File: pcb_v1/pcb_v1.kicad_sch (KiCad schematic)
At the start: 13 parts, among them J3 Conn_01x07, SW1 SW_Push, SW2 SW_Push, U2 SRV05-4, U3 IQS624-3200-DNR

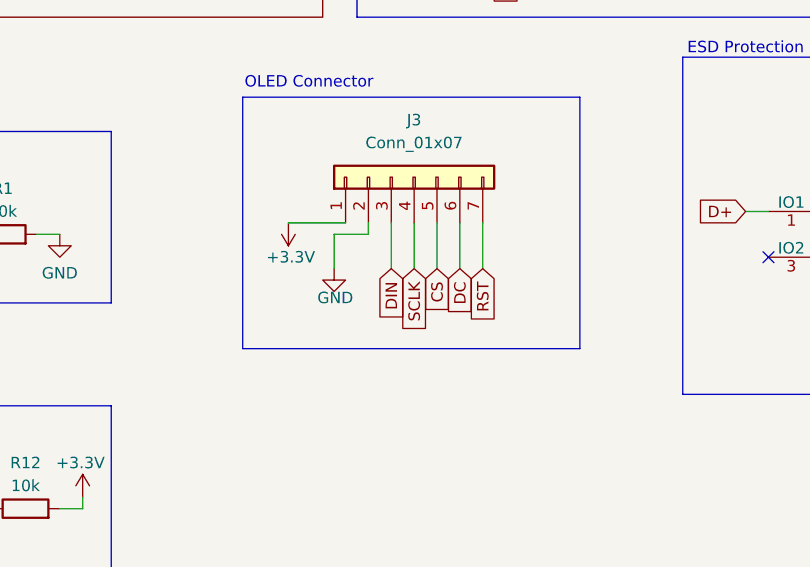
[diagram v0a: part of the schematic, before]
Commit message: Reverse polarity on pins
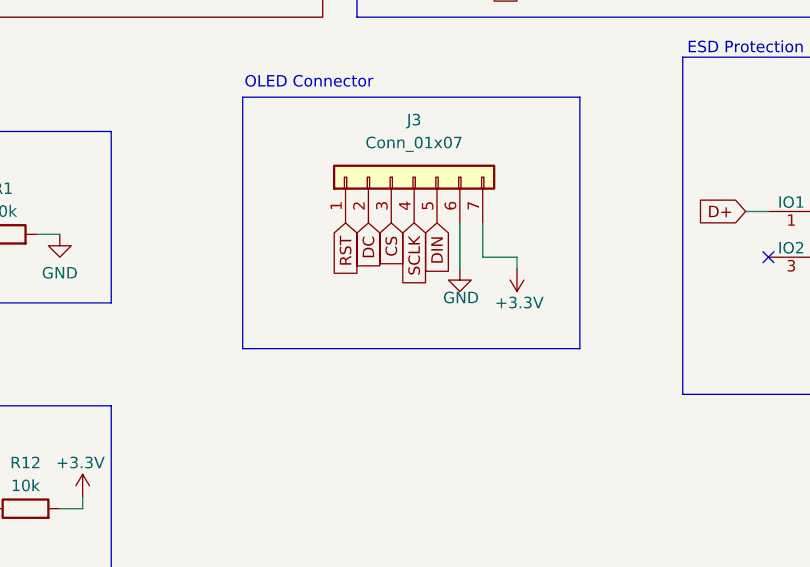
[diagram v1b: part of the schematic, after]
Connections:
- net +3.3V: now also J3.7 (Pin_7); no longer J3.1 (Pin_1)
- net CS: now also J3.3 (Pin_3); no longer J3.5 (Pin_5)
- net DC: now also J3.2 (Pin_2); no longer J3.6 (Pin_6)
- net DIN: now also J3.5 (Pin_5); no longer J3.3 (Pin_3)
- net GND: now also J3.6 (Pin_6); no longer J3.2 (Pin_2)
- net RST: now also J3.1 (Pin_1); no longer J3.7 (Pin_7)
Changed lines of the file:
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@@
 	(wire
 		(pts
-			(xy 196.85 149.86) (xy 196.85 144.78)
+			(xy 200.66 149.86) (xy 200.66 148.59)
 		)
 		(stroke
@@
 	(wire
 		(pts
+			(xy 200.66 148.59) (xy 196.85 148.59)
+		)
+		(stroke
+			(width 0)
+			(type default)
+		)
+	)
+	(wire
+		(pts
 			(xy 265.43 114.3) (xy 265.43 113.03)
 		)
@@
 	(wire
 		(pts
-			(xy 186.69 144.78) (xy 186.69 149.86)
-		)
-		(stroke
-			(width 0)
-			(type default)
-		)
-	)
-	(wire
-		(pts
 			(xy 186.69 101.6) (xy 199.39 101.6)
 		)
@@
 	(wire
 		(pts
-			(xy 191.77 149.86) (xy 191.77 144.78)
-		)
-		(stroke
-			(width 0)
-			(type default)
-		)
-	)
-	(wire
-		(pts
 			(xy 194.31 99.06) (xy 194.31 95.25)
 		)
@@
 	(wire
 		(pts
-			(xy 175.26 144.78) (xy 181.61 144.78)
-		)
-		(stroke
-			(width 0)
-			(type default)
-		)
-	)
-	(wire
-		(pts
 			(xy 241.3 158.75) (xy 247.65 158.75)
 		)
@@
 	(wire
 		(pts
-			(xy 180.34 146.05) (xy 184.15 146.05)
-		)
-		(stroke
-			(width 0)
-			(type default)
-		)
-	)
-	(wire
-		(pts
 			(xy 265.43 109.22) (xy 265.43 113.03)
 		)
@@
 	(wire
 		(pts
-			(xy 189.23 149.86) (xy 189.23 144.78)
-		)
-		(stroke
-			(width 0)
-			(type default)
-		)
-	)
-	(wire
-		(pts
 			(xy 205.74 96.52) (xy 204.47 96.52)
 		)
@@
 	(wire
 		(pts
-			(xy 184.15 146.05) (xy 184.15 144.78)
-		)
-		(stroke
-			(width 0)
-			(type default)
-		)
-	)
-	(wire
-		(pts
 			(xy 226.06 143.51) (xy 228.6 143.51)
 		)
@@
 	(wire
 		(pts
+			(xy 196.85 148.59) (xy 196.85 144.78)
+		)
+		(stroke
+			(width 0)
+			(type default)
+		)
+	)
+	(wire
+		(pts
 			(xy 139.7 173.99) (xy 139.7 176.53)
 		)
@@
 	(wire
 		(pts
-			(xy 180.34 149.86) (xy 180.34 146.05)
-		)
-		(stroke
-			(width 0)
-			(type default)
-		)
-	)
-	(wire
-		(pts
 			(xy 252.73 113.03) (xy 252.73 109.22)
 		)
@@
 			(width 0)
 			(type default)
-		)
-	)
-	(global_label "CS"
-		(shape input)
-		(at 191.77 149.86 270)
-		(fields_autoplaced yes)
-		(effects
-			(font
-				(size 1.27 1.27)
-			)
-			(justify right)
-		)
-		(property "Intersheetrefs" "${INTERSHEET_REFS}"
-			(at 191.77 155.3247 90)
-			(effects
-				(font
-					(size 1.27 1.27)
-				)
-				(justify right)
-				(hide yes)
-			)
 		)
 	)
@@
 		)
 	)
+	(global_label "DIN"
+		(shape input)
+		(at 191.77 144.78 270)
+		(fields_autoplaced yes)
+		(effects
+			(font
+				(size 1.27 1.27)
+			)
+			(justify right)
+		)
+		(property "Intersheetrefs" "${INTERSHEET_REFS}"
+			(at 191.77 150.9705 90)
+			(effects
+				(font
+					(size 1.27 1.27)
+				)
+				(justify right)
+				(hide yes)
+			)
+		)
+	)
 	(global_label "RDY"
 		(shape input)
@@
 		)
 	)
-	(global_label "DIN"
-		(shape input)
-		(at 186.69 149.86 270)
-		(fields_autoplaced yes)
-		(effects
-			(font
-				(size 1.27 1.27)
-			)
-			(justify right)
-		)
-		(property "Intersheetrefs" "${INTERSHEET_REFS}"
-			(at 186.69 156.0505 90)
-			(effects
-				(font
-					(size 1.27 1.27)
-				)
-				(justify right)
-				(hide yes)
-			)
-		)
-	)
 	(global_label "D+"
 		(shape input)
@@
 		)
 	)
-	(global_label "DC"
+	(global_label "CS"
 		(shape input)
-		(at 194.31 149.86 270)
+		(at 186.69 144.78 270)
 		(fields_autoplaced yes)
 		(effects
@@
 		)
 		(property "Intersheetrefs" "${INTERSHEET_REFS}"
-			(at 194.31 155.3852 90)
+			(at 186.69 150.2447 90)
+			(effects
+				(font
+					(size 1.27 1.27)
+				)
+				(justify right)
+				(hide yes)
+			)
+		)
+	)
+	(global_label "RST"
+		(shape input)
+		(at 181.61 144.78 270)
+		(fields_autoplaced yes)
+		(effects
+			(font
+				(size 1.27 1.27)
+			)
+			(justify right)
+		)
+		(property "Intersheetrefs" "${INTERSHEET_REFS}"
+			(at 181.61 151.2123 90)
+			(effects
+				(font
+					(size 1.27 1.27)
+				)
+				(justify right)
+				(hide yes)
+			)
+		)
+	)
+	(global_label "DC"
+		(shape input)
+		(at 184.15 144.78 270)
+		(fields_autoplaced yes)
+		(effects
+			(font
+				(size 1.27 1.27)
+			)
+			(justify right)
+		)
+		(property "Intersheetrefs" "${INTERSHEET_REFS}"
+			(at 184.15 150.3052 90)
 			(effects
 				(font
@@
 		)
 	)
-	(global_label "RST"
-		(shape input)
-		(at 196.85 149.86 270)
-		(fields_autoplaced yes)
-		(effects
-			(font
-				(size 1.27 1.27)
-			)
-			(justify right)
-		)
-		(property "Intersheetrefs" "${INTERSHEET_REFS}"
-			(at 196.85 156.2923 90)
-			(effects
-				(font
-					(size 1.27 1.27)
-				)
-				(justify right)
-				(hide yes)
-			)
-		)
-	)
 	(global_label "SDA"
 		(shape input)
@@
 	(global_label "SCLK"
 		(shape input)
-		(at 189.23 149.86 270)
+		(at 189.23 144.78 270)
 		(fields_autoplaced yes)
 		(effects
@@
 		)
 		(property "Intersheetrefs" "${INTERSHEET_REFS}"
-			(at 189.23 157.6228 90)
+			(at 189.23 152.5428 90)
 			(effects
 				(font
@@
 	(symbol
 		(lib_id "power:GND")
-		(at 180.34 149.86 0)
+		(at 194.31 149.86 0)
 		(unit 1)
 		(exclude_from_sim no)
@@
 		(dnp no)
 		(property "Reference" "#PWR011"
-			(at 180.34 156.21 0)
+			(at 194.31 156.21 0)
 			(effects
 				(font
@@
 		)
 		(property "Value" "GND"
-			(at 180.467 153.1112 0)
+			(at 194.437 153.1112 0)
 			(effects
 				(font
@@
 		)
 		(property "Footprint" ""
-			(at 180.34 149.86 0)
+			(at 194.31 149.86 0)
 			(effects
 				(font
@@
 		)
 		(property "Datasheet" ""
-			(at 180.34 149.86 0)
+			(at 194.31 149.86 0)
 			(effects
 				(font
@@
 		)
 		(property "Description" ""
-			(at 180.34 149.86 0)
+			(at 194.31 149.86 0)
 			(effects
 				(font
@@
 	(symbol
 		(lib_id "power:+3.3V")
-		(at 175.26 144.78 180)
+		(at 200.66 149.86 180)
 		(unit 1)
 		(exclude_from_sim no)
@@
 		(dnp no)
 		(property "Reference" "#PWR0227"
-			(at 175.26 140.97 0)
+			(at 200.66 146.05 0)
 			(effects
 				(font
@@
 		)
 		(property "Value" "+3.3V"
-			(at 175.514 148.59 0)
+			(at 200.914 153.67 0)
 			(effects
 				(font
@@
 		)
 		(property "Footprint" ""
-			(at 175.26 144.78 0)
+			(at 200.66 149.86 0)
 			(effects
 				(font
@@
 		)
 		(property "Datasheet" ""
-			(at 175.26 144.78 0)
+			(at 200.66 149.86 0)
 			(effects
 				(font
@@
 		)
 		(property "Description" "Power symbol creates a global label with name \"+3.3V\""
-			(at 175.26 144.78 0)
-			(effects
-				(font
+			(at 200.66 149.86 0)
+			(effects
+				(font
